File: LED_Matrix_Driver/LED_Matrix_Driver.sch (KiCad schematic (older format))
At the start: 65 parts, among them J1 Screw_Terminal_01x02, J2 LED Anode Rows, J3 Columns 24-31 LED Cathodes, J4 Columns 16-23 LED Cathodes, J5 Columns 8-15 LED Cathodes, J6 Columns 0-7 LED Cathodes, U1 ESP32-DEVKITC-32E, U2 74HCT244, U3 MIC2981, U4 74HC238, U5 HEF4794B, U6 HEF4794B, U7 HEF4794B, U8 HEF4794B

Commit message: Created a new PCB layout for LEDMatrixDriver board
- More compact
- Removed unused capacitors
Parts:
- removed C1, C2, C3, C4: 0.1uF, Capacitor_THT:C_Axial_L3.8mm_D2.6mm_P7.50mm_Horizontal, symbol Device:C_Small
- R1, R10, R11, R12, R13, R14, R15, R16, R17, R18, R19, R2, R20, R21, R22, R23, R24, R25, R26, R27, R28, R29, R3, R30, R31, R32, R33, R34, R35, R36, R37, R38, R39, R4, R40, R41, R42, R43, R44, R45, R46, R47, R5, R6, R7, R8, R9: footprint Resistor_THT:R_Axial_DIN0204_L3.6mm_D1.6mm_P7.62mm_Horizontal -> Resistor_THT:R_Axial_DIN0207_L6.3mm_D2.5mm_P10.16mm_Horizontal
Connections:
- net +5V: now also U1.19 (5V)

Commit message: Modified design to include decoupling capacitors. PCB is now 4 layers with power and ground planes
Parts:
- added C1, C2, C3, C4, C5, C6, C7: 0.1uF, Capacitor_THT:C_Rect_L7.0mm_W2.0mm_P5.00mm, symbol Device:C_Small
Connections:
- net +5V: now also C1.2, C2.2, C3.1, C4.1, C5.1, C6.1, C7.1
- net Earth: now also C1.1, C2.1, C3.2, C4.2, C5.2, C6.2, C7.2
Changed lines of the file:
@@
 	8350 1900 8350 900
-Wire Wire Line
-	6850 6300 6850 6150
 Wire Wire Line
 	7550 6300 7550 6150
@@
 Connection ~ 6500 2350
 Wire Wire Line
-	6500 2450 6500 2350
+	6500 2450 6500 2400
 $Comp
 L power:+5V #PWR06
@@
 Connection ~ 7300 2850
 Wire Wire Line
-	7600 3450 7700 3450
+	7600 3450 7650 3450
 $Comp
 L power:Earth #PWR08
 U 1 1 65533632
-P 6550 3500
-F 0 "#PWR08" H 6550 3250 50  0001 C CNN
-F 1 "Earth" H 6550 3350 50  0001 C CNN
-F 2 "" H 6550 3500 50  0001 C CNN
-F 3 "~" H 6550 3500 50  0001 C CNN
-	1    6550 3500
+P 6550 4100
+F 0 "#PWR08" H 6550 3850 50  0001 C CNN
+F 1 "Earth" H 6550 3950 50  0001 C CNN
+F 2 "" H 6550 4100 50  0001 C CNN
+F 3 "~" H 6550 4100 50  0001 C CNN
+	1    6550 4100
 	1    0    0    -1
 $EndComp
@@
 Wire Wire Line
 	6550 2850 7300 2850
-Wire Wire Line
-	6550 3500 6550 3450
 Wire Wire Line
 	7700 3450 7700 3400
@@
 	5000 3050 5650 3050
 Wire Wire Line
-	8150 2000 8150 3350
-Wire Wire Line
-	8150 3350 8150 4700
-Wire Wire Line
-	8150 4700 8150 6050
+	8150 2000 8150 3250
+Wire Wire Line
+	8150 3350 8150 4600
+Wire Wire Line
+	8150 4700 8150 5950
+$Comp
+L Device:C_Small C1
+U 1 1 656ACBE6
+P 6700 750
+F 0 "C1" V 6471 750 50  0000 C CNN
+F 1 "0.1uF" V 6562 750 50  0000 C CNN
+F 2 "Capacitor_THT:C_Rect_L7.0mm_W2.0mm_P5.00mm" H 6700 750 50  0001 C CNN
+F 3 "~" H 6700 750 50  0001 C CNN
+	1    6700 750
+	0    1    1    0
+$EndComp
+Wire Wire Line
+	7300 2400 6500 2400
+Connection ~ 6500 2400
+Wire Wire Line
+	6500 2400 6500 2350
+$Comp
+L Device:C_Small C4
+U 1 1 656DD45F
+P 8250 1900
+F 0 "C4" V 8021 1900 50  0000 C CNN
+F 1 "0.1uF" V 8112 1900 50  0000 C CNN
+F 2 "Capacitor_THT:C_Rect_L7.0mm_W2.0mm_P5.00mm" H 8250 1900 50  0001 C CNN
+F 3 "~" H 8250 1900 50  0001 C CNN
+	1    8250 1900
+	0    1    1    0
+$EndComp
+$Comp
+L Device:C_Small C5
+U 1 1 656DE70C
+P 8250 3250
+F 0 "C5" V 8021 3250 50  0000 C CNN
+F 1 "0.1uF" V 8112 3250 50  0000 C CNN
+F 2 "Capacitor_THT:C_Rect_L7.0mm_W2.0mm_P5.00mm" H 8250 3250 50  0001 C CNN
+F 3 "~" H 8250 3250 50  0001 C CNN
+	1    8250 3250
+	0    1    1    0
+$EndComp
+Connection ~ 8150 3250
+Wire Wire Line
+	8150 3250 8150 3350
+$Comp
+L Device:C_Small C6
+U 1 1 656DF0C7
+P 8250 4600
+F 0 "C6" V 8021 4600 50  0000 C CNN
+F 1 "0.1uF" V 8112 4600 50  0000 C CNN
+F 2 "Capacitor_THT:C_Rect_L7.0mm_W2.0mm_P5.00mm" H 8250 4600 50  0001 C CNN
+F 3 "~" H 8250 4600 50  0001 C CNN
+	1    8250 4600
+	0    1    1    0
+$EndComp
+Connection ~ 8150 4600
+Wire Wire Line
+	8150 4600 8150 4700
+$Comp
+L Device:C_Small C7
+U 1 1 656DFE0F
+P 8250 5950
+F 0 "C7" V 8021 5950 50  0000 C CNN
+F 1 "0.1uF" V 8112 5950 50  0000 C CNN
+F 2 "Capacitor_THT:C_Rect_L7.0mm_W2.0mm_P5.00mm" H 8250 5950 50  0001 C CNN
+F 3 "~" H 8250 5950 50  0001 C CNN
+	1    8250 5950
+	0    1    1    0
+$EndComp
+Connection ~ 8350 5950
+Connection ~ 8150 5950
+Wire Wire Line
+	8150 5950 8150 6050
+$Comp
+L Device:C_Small C2
+U 1 1 656E07C6
+P 7200 6300
+F 0 "C2" V 7300 6200 50  0000 C CNN
+F 1 "0.1uF" V 7300 6400 50  0000 C CNN
+F 2 "Capacitor_THT:C_Rect_L7.0mm_W2.0mm_P5.00mm" H 7200 6300 50  0001 C CNN
+F 3 "~" H 7200 6300 50  0001 C CNN
+	1    7200 6300
+	0    1    1    0
+$EndComp
+Wire Wire Line
+	6850 6300 6850 6150
+Wire Wire Line
+	7100 6300 6850 6300
+Connection ~ 6850 6300
+Wire Wire Line
+	7300 6300 7550 6300
+Connection ~ 7550 6300
+$Comp
+L Device:C_Small C3
+U 1 1 6572E66B
+P 7650 3600
+F 0 "C3" H 7700 3700 50  0000 L CNN
+F 1 "0.1uF" H 7700 3500 50  0000 L CNN
+F 2 "Capacitor_THT:C_Rect_L7.0mm_W2.0mm_P5.00mm" H 7650 3600 50  0001 C CNN
+F 3 "~" H 7650 3600 50  0001 C CNN
+	1    7650 3600
+	1    0    0    -1
+$EndComp
+Wire Wire Line
+	7650 3500 7650 3450
+Connection ~ 7650 3450
+Wire Wire Line
+	7650 3450 7700 3450
+Wire Wire Line
+	6550 4050 7650 4050
+Wire Wire Line
+	7650 4050 7650 3700
+Wire Wire Line
+	6550 3450 6550 4050
+Wire Wire Line
+	6550 4100 6550 4050
+Connection ~ 6550 4050
+Wire Wire Line
+	8150 2000 8150 1900
+Connection ~ 8150 2000
+Wire Wire Line
+	6600 750  6500 750
+Connection ~ 6500 750
+Wire Wire Line
+	6800 750  7300 750
+Wire Wire Line
+	7300 750  7300 2400
 $EndSCHEMATC

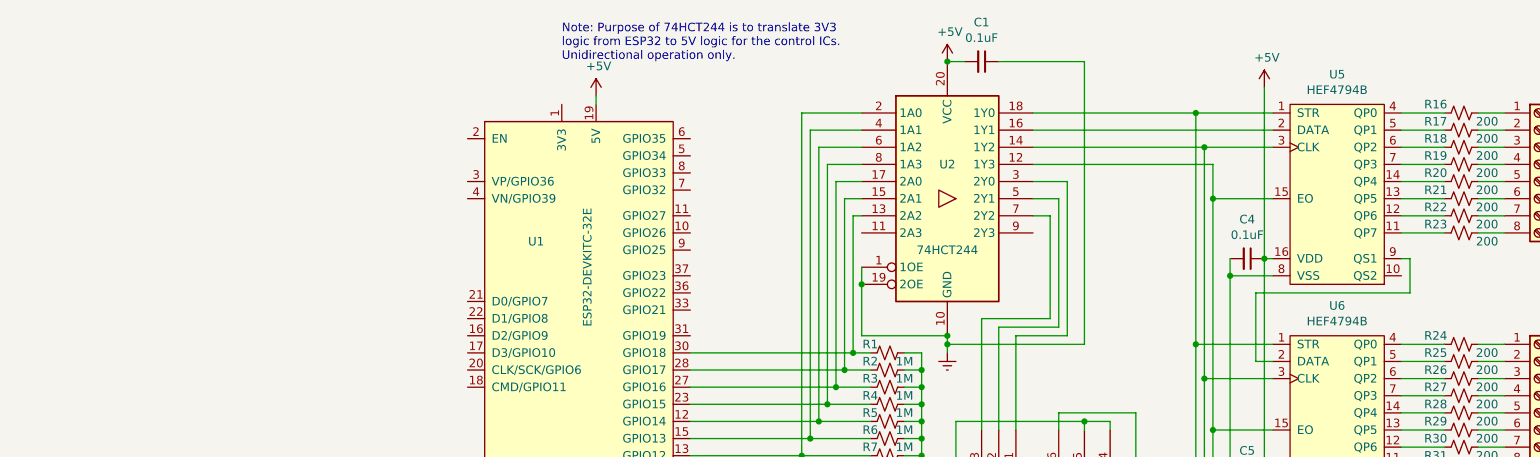
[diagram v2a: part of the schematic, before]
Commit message: Added 6 push buttons to the PCB as well as 4 mounting holes
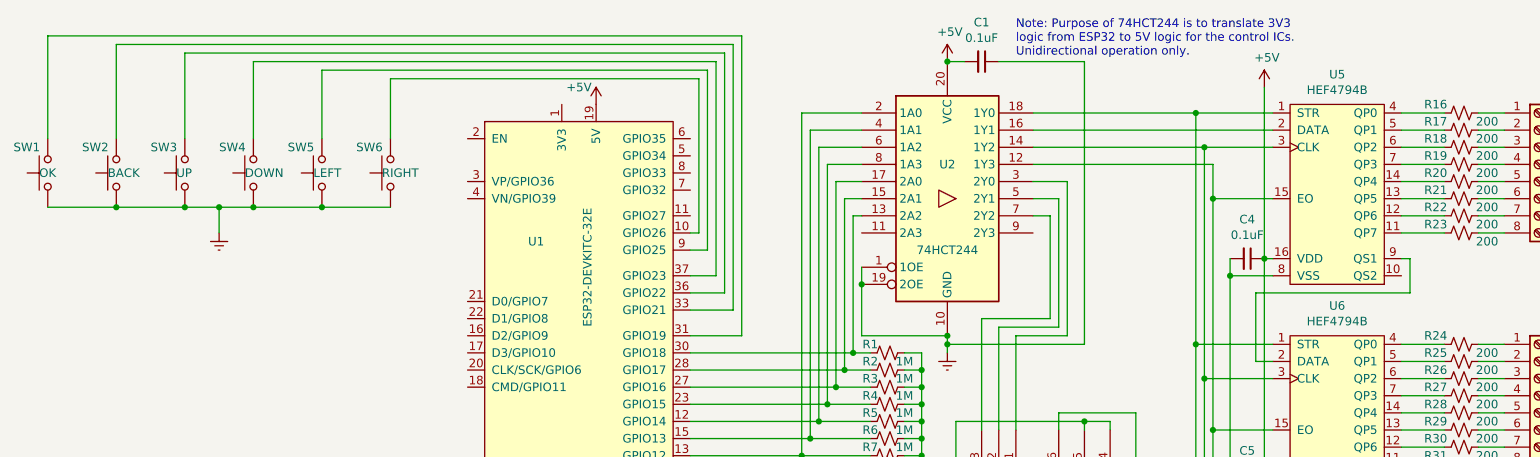
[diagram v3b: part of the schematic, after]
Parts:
- added SW1: OK, Arduino:Custom_Pin_Header, symbol Switch:SW_Push
- added SW2: BACK, Arduino:Custom_Pin_Header, symbol Switch:SW_Push
- added SW3: UP, Arduino:Custom_Pin_Header, symbol Switch:SW_Push
- added SW4: DOWN, Arduino:Custom_Pin_Header, symbol Switch:SW_Push
- added SW5: LEFT, Arduino:Custom_Pin_Header, symbol Switch:SW_Push
- added SW6: RIGHT, Arduino:Custom_Pin_Header, symbol Switch:SW_Push
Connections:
- net Earth: now also SW1.2, SW2.2, SW3.2, SW4.2, SW5.2, SW6.2
- net at U1.10 (GPIO26): now also SW6.1
- net at U1.31 (GPIO19): now also SW1.1
- net at U1.33 (GPIO21): now also SW2.1
- net at U1.36 (GPIO22): now also SW3.1
- net at U1.37 (GPIO23): now also SW4.1
- net at U1.9 (GPIO25): now also SW5.1
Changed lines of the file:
@@
 Wire Wire Line
 	6250 3050 6350 3050
-Wire Wire Line
-	5650 3050 6050 3050
-Connection ~ 5700 2950
-Wire Wire Line
-	5700 2950 6050 2950
-Connection ~ 5750 2850
-Wire Wire Line
-	6050 2850 5750 2850
-Connection ~ 5800 2750
-Wire Wire Line
-	5800 2750 6050 2750
-Connection ~ 5850 2650
-Wire Wire Line
-	6050 2650 5850 2650
-Connection ~ 5900 2550
-Wire Wire Line
-	5900 2550 6050 2550
-Connection ~ 5950 2450
-Wire Wire Line
-	6050 2450 5950 2450
 $Comp
 L Device:R_Small_US R1
@@
 	0    -1   -1   0
 $EndComp
-Connection ~ 5650 3050
 $Comp
 L Device:R_Small_US R7
@@
 	0    -1   -1   0
 $EndComp
-Text Notes 4250 750  0    50   ~ 0
+Text Notes 6900 725  0    50   ~ 0
 Note: Purpose of 74HCT244 is to translate 3V3 \nlogic from ESP32 to 5V logic for the control ICs. \nUnidirectional operation only.
 Wire Wire Line
@@
 Wire Wire Line
 	4350 3800 4350 3850
-Wire Wire Line
-	4450 950  4450 1000
 $Comp
 L power:+5V #PWR03
 U 1 1 6580F9E1
-P 4450 950
-F 0 "#PWR03" H 4450 800 50  0001 C CNN
-F 1 "+5V" H 4465 1123 50  0000 C CNN
-F 2 "" H 4450 950 50  0001 C CNN
-F 3 "" H 4450 950 50  0001 C CNN
-	1    4450 950
+P 4450 1000
+F 0 "#PWR03" H 4450 850 50  0001 C CNN
+F 1 "+5V" H 4350 1100 50  0000 C CNN
+F 2 "" H 4450 1000 50  0001 C CNN
+F 3 "" H 4450 1000 50  0001 C CNN
+	1    4450 1000
 	1    0    0    -1
 $EndComp
@@
 	5650 1050 6000 1050
 Wire Wire Line
-	5650 1050 5650 3050
-Wire Wire Line
 	6000 1150 5700 1150
 Wire Wire Line
-	5700 1150 5700 2950
-Wire Wire Line
 	5750 1250 6000 1250
 Wire Wire Line
-	5750 1250 5750 2850
-Wire Wire Line
 	6000 1350 5800 1350
 Wire Wire Line
-	5800 1350 5800 2750
-Wire Wire Line
 	5850 1450 6000 1450
 Wire Wire Line
-	5850 1450 5850 2650
-Wire Wire Line
 	5900 1550 6000 1550
 Wire Wire Line
-	5900 1550 5900 2550
-Wire Wire Line
 	5950 1650 6000 1650
-Wire Wire Line
-	5950 1650 5950 2450
 $Comp
 L Connector:Screw_Terminal_01x02 J1
@@
 Wire Wire Line
 	4850 6100 4950 6100
-$Comp
-L Custom_Symbols:ESP32-DEVKITC-32E U1
-U 1 1 6539A849
-P 4350 2400
-F 0 "U1" H 4100 3000 50  0000 C CNN
-F 1 "ESP32-DEVKITC-32E" V 4400 2850 50  0000 C CNN
-F 2 "Arduino:ESP32-DevkitC" H 4300 2400 50  0001 C CNN
-F 3 "" H 4300 2400 50  0001 C CNN
-	1    4350 2400
-	1    0    0    -1
-$EndComp
-Wire Wire Line
-	5000 2450 5950 2450
-Wire Wire Line
-	5000 2550 5900 2550
-Wire Wire Line
-	5000 2650 5850 2650
-Wire Wire Line
-	5000 2750 5800 2750
-Wire Wire Line
-	5000 2850 5750 2850
-Wire Wire Line
-	5000 2950 5700 2950
-Wire Wire Line
-	5000 3050 5650 3050
 Wire Wire Line
 	8150 2000 8150 3250
@@
 Wire Wire Line
 	7300 750  7300 2400
+Wire Wire Line
+	5850 1450 5850 2650
+Wire Wire Line
+	5950 1650 5950 2450
+Wire Wire Line
+	5900 1550 5900 2550
+Wire Wire Line
+	5800 1350 5800 2750
+Wire Wire Line
+	5650 3050 6050 3050
+Wire Wire Line
+	5700 2950 6050 2950
+Wire Wire Line
+	6050 2850 5750 2850
+Wire Wire Line
+	5800 2750 6050 2750
+Wire Wire Line
+	6050 2650 5850 2650
+Wire Wire Line
+	5900 2550 6050 2550
+Wire Wire Line
+	6050 2450 5950 2450
+Wire Wire Line
+	5750 1250 5750 2850
+Wire Wire Line
+	5700 1150 5700 2950
+Wire Wire Line
+	5650 1050 5650 3050
+Connection ~ 5650 3050
+Wire Wire Line
+	5000 3050 5650 3050
+Connection ~ 5700 2950
+Wire Wire Line
+	5000 2950 5700 2950
+Connection ~ 5750 2850
+Wire Wire Line
+	5000 2850 5750 2850
+Connection ~ 5800 2750
+Wire Wire Line
+	5000 2750 5800 2750
+Connection ~ 5850 2650
+Wire Wire Line
+	5000 2650 5850 2650
+Connection ~ 5900 2550
+Wire Wire Line
+	5000 2550 5900 2550
+Connection ~ 5950 2450
+Wire Wire Line
+	5000 2450 5950 2450
+$Comp
+L Custom_Symbols:ESP32-DEVKITC-32E U1
+U 1 1 6539A849
+P 4350 2400
+F 0 "U1" H 4100 3000 50  0000 C CNN
+F 1 "ESP32-DEVKITC-32E" V 4400 2850 50  0000 C CNN
+F 2 "Arduino:ESP32-DevkitC" H 4300 2400 50  0001 C CNN
+F 3 "" H 4300 2400 50  0001 C CNN
+	1    4350 2400
+	1    0    0    -1
+$EndComp
+$Comp
+L Switch:SW_Push SW6
+U 1 1 658676FC
+P 3250 1400
+F 0 "SW6" V 3100 1600 50  0000 R CNN
+F 1 "RIGHT" V 3250 1450 50  0000 R CNN
+F 2 "Arduino:Custom_Pin_Header" H 3250 1600 50  0001 C CNN
+F 3 "~" H 3250 1600 50  0001 C CNN
+	1    3250 1400
+	0    -1   1    0
+$EndComp
+$Comp
+L Switch:SW_Push SW5
+U 1 1 6586BF68
+P 2850 1400
+F 0 "SW5" V 2700 1600 50  0000 R CNN
+F 1 "LEFT" V 2850 1450 50  0000 R CNN
+F 2 "Arduino:Custom_Pin_Header" H 2850 1600 50  0001 C CNN
+F 3 "~" H 2850 1600 50  0001 C CNN
+	1    2850 1400
+	0    -1   1    0
+$EndComp
+$Comp
+L Switch:SW_Push SW4
+U 1 1 6586C49E
+P 2450 1400
+F 0 "SW4" V 2300 1600 50  0000 R CNN
+F 1 "DOWN" V 2450 1450 50  0000 R CNN
+F 2 "Arduino:Custom_Pin_Header" H 2450 1600 50  0001 C CNN
+F 3 "~" H 2450 1600 50  0001 C CNN
+	1    2450 1400
+	0    -1   1    0
+$EndComp
+$Comp
+L Switch:SW_Push SW3
+U 1 1 6586C73A
+P 2050 1400
+F 0 "SW3" V 1900 1600 50  0000 R CNN
+F 1 "UP" V 2050 1450 50  0000 R CNN
+F 2 "Arduino:Custom_Pin_Header" H 2050 1600 50  0001 C CNN
+F 3 "~" H 2050 1600 50  0001 C CNN
+	1    2050 1400
+	0    -1   1    0
+$EndComp
+$Comp
+L Switch:SW_Push SW2
+U 1 1 6586CCB3
+P 1650 1400
+F 0 "SW2" V 1500 1600 50  0000 R CNN
+F 1 "BACK" V 1650 1450 50  0000 R CNN
+F 2 "Arduino:Custom_Pin_Header" H 1650 1600 50  0001 C CNN
+F 3 "~" H 1650 1600 50  0001 C CNN
+	1    1650 1400
+	0    -1   1    0
+$EndComp
+$Comp
+L Switch:SW_Push SW1
+U 1 1 6590598D
+P 1250 1400
+F 0 "SW1" V 1100 1600 50  0000 R CNN
+F 1 "OK" V 1250 1450 50  0000 R CNN
+F 2 "Arduino:Custom_Pin_Header" H 1250 1600 50  0001 C CNN
+F 3 "~" H 1250 1600 50  0001 C CNN
+	1    1250 1400
+	0    -1   1    0
+$EndComp
+Wire Wire Line
+	3250 1200 3250 850
+Wire Wire Line
+	3250 850  5050 850
+Wire Wire Line
+	5050 850  5050 1750
+Wire Wire Line
+	5050 1750 5000 1750
+Wire Wire Line
+	2850 1200 2850 800
+Wire Wire Line
+	2850 800  5100 800
+Wire Wire Line
+	5100 800  5100 1850
+Wire Wire Line
+	5100 1850 5000 1850
+Wire Wire Line
+	2450 1200 2450 750
+Wire Wire Line
+	2450 750  5150 750
+Wire Wire Line
+	5150 750  5150 2000
+Wire Wire Line
+	5150 2000 5000 2000
+Wire Wire Line
+	2050 1200 2050 700
+Wire Wire Line
+	2050 700  5200 700
+Wire Wire Line
+	5200 700  5200 2100
+Wire Wire Line
+	5200 2100 5000 2100
+Wire Wire Line
+	5000 2200 5250 2200
+Wire Wire Line
+	5250 2200 5250 650
+Wire Wire Line
+	5250 650  1650 650
+Wire Wire Line
+	1650 650  1650 1200
+Wire Wire Line
+	1250 1200 1250 600
+Wire Wire Line
+	1250 600  5300 600
+Wire Wire Line
+	5300 600  5300 2350
+Wire Wire Line
+	5300 2350 5000 2350
+Wire Wire Line
+	1250 1600 1650 1600
+Connection ~ 2850 1600
+Wire Wire Line
+	2850 1600 3250 1600
+Connection ~ 2450 1600
+Wire Wire Line
+	2450 1600 2850 1600
+Connection ~ 1650 1600
+Wire Wire Line
+	1650 1600 2050 1600
+Wire Wire Line
+	2050 1600 2250 1600
+Connection ~ 2050 1600
+Wire Wire Line
+	2250 1600 2250 1750
+Connection ~ 2250 1600
+Wire Wire Line
+	2250 1600 2450 1600
+$Comp
+L power:Earth #PWR014
+U 1 1 65AE4D92
+P 2250 1750
+F 0 "#PWR014" H 2250 1500 50  0001 C CNN
+F 1 "Earth" H 2250 1600 50  0001 C CNN
+F 2 "" H 2250 1750 50  0001 C CNN
+F 3 "~" H 2250 1750 50  0001 C CNN
+	1    2250 1750
+	1    0    0    -1
+$EndComp
 $EndSCHEMATC

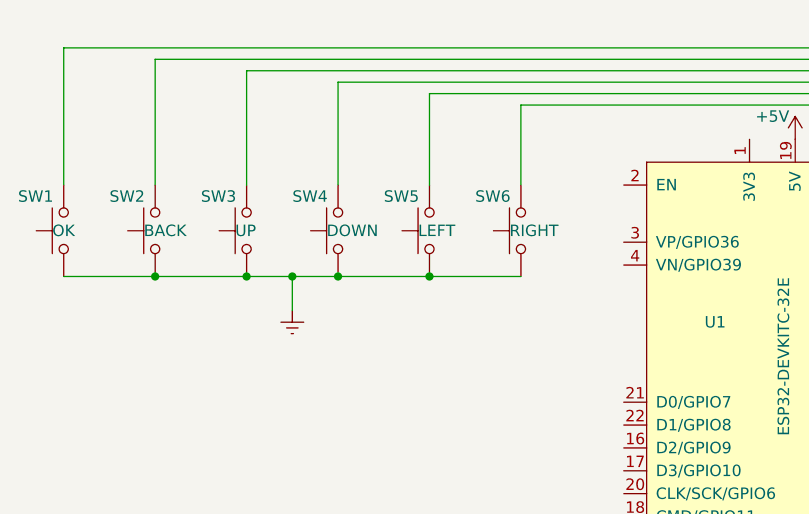
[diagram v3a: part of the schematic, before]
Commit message: Updated the PCB. Now includes solder points for a few buttons
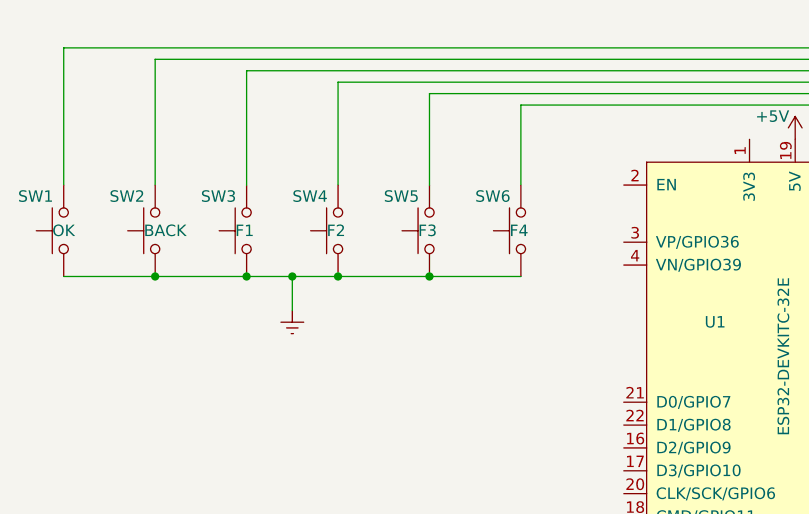
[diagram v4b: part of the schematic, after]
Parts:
- SW3: value UP -> F1
- SW4: value DOWN -> F2
- SW5: value LEFT -> F3
- SW6: value RIGHT -> F4
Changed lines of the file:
@@
 P 3250 1400
 F 0 "SW6" V 3100 1600 50  0000 R CNN
-F 1 "RIGHT" V 3250 1450 50  0000 R CNN
+F 1 "F4" V 3250 1450 50  0000 R CNN
 F 2 "Arduino:Custom_Pin_Header" H 3250 1600 50  0001 C CNN
 F 3 "~" H 3250 1600 50  0001 C CNN
@@
 P 2850 1400
 F 0 "SW5" V 2700 1600 50  0000 R CNN
-F 1 "LEFT" V 2850 1450 50  0000 R CNN
+F 1 "F3" V 2850 1450 50  0000 R CNN
 F 2 "Arduino:Custom_Pin_Header" H 2850 1600 50  0001 C CNN
 F 3 "~" H 2850 1600 50  0001 C CNN
@@
 P 2450 1400
 F 0 "SW4" V 2300 1600 50  0000 R CNN
-F 1 "DOWN" V 2450 1450 50  0000 R CNN
+F 1 "F2" V 2450 1450 50  0000 R CNN
 F 2 "Arduino:Custom_Pin_Header" H 2450 1600 50  0001 C CNN
 F 3 "~" H 2450 1600 50  0001 C CNN
@@
 P 2050 1400
 F 0 "SW3" V 1900 1600 50  0000 R CNN
-F 1 "UP" V 2050 1450 50  0000 R CNN
+F 1 "F1" V 2050 1450 50  0000 R CNN
 F 2 "Arduino:Custom_Pin_Header" H 2050 1600 50  0001 C CNN
 F 3 "~" H 2050 1600 50  0001 C CNN
